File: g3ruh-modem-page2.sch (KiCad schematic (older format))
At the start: 48 parts, among them J8 CONN_01X02, P1 CONN_01X03, P2 CONN_01X06, P3 CONN_01X05, P4 C96ABC, U11 74HC14, U13 74HC86, U14 74HC164, U15 27C128, U16 TL084, U17 74HC74, U18 74HC164, U19 ZN429E-8

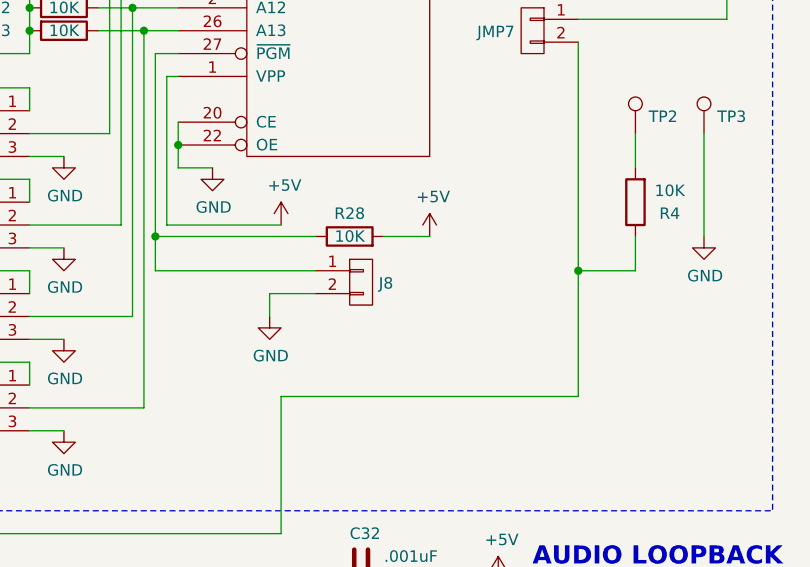
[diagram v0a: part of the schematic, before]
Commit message: Parts in roughly the right places and footprints verified.
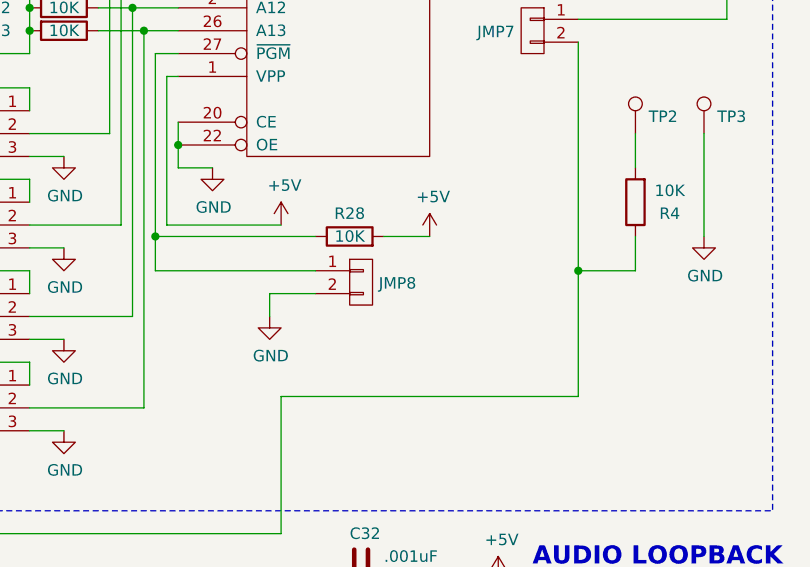
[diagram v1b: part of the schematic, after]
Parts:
- C29, C30, C31, C32: footprint Capacitors_THT:C_Disc_D3.0mm_W2.0mm_P2.50mm -> Capacitors_THT:C_Axial_L3.8mm_D2.6mm_P10.00mm_Horizontal
- renumbered J8 to JMP8
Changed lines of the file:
@@
 $EndComp
 $Comp
-L CONN_01X02 J8
+L CONN_01X02 JMP8
 U 1 1 596FAC32
 P 9350 3200
-F 0 "J8" H 9427 3195 50  0000 L CNN
+F 0 "JMP8" H 9427 3195 50  0000 L CNN
 F 1 "CONN_01X02" H 9428 3150 50  0001 L CNN
 F 2 "Pin_Headers:Pin_Header_Straight_1x02_Pitch2.54mm" H 9350 3200 50  0001 C CNN
@@
 F 0 "C32" V 9200 4400 50  0000 L CNN
 F 1 ".001uF" V 9300 4550 50  0000 L CNN
-F 2 "Capacitors_THT:C_Disc_D3.0mm_W2.0mm_P2.50mm" H 9388 4300 50  0001 C CNN
+F 2 "Capacitors_THT:C_Axial_L3.8mm_D2.6mm_P10.00mm_Horizontal" H 9388 4300 50  0001 C CNN
 F 3 "" H 9350 4450 50  0001 C CNN
 F 4 "2.5% polystyrene" H 9350 4450 60  0001 C CNN "Type"
@@
 F 0 "C30" H 7050 5200 50  0000 L CNN
 F 1 "100pF" H 7000 5100 50  0000 L CNN
-F 2 "Capacitors_THT:C_Disc_D3.0mm_W2.0mm_P2.50mm" H 6938 5000 50  0001 C CNN
+F 2 "Capacitors_THT:C_Axial_L3.8mm_D2.6mm_P10.00mm_Horizontal" H 6938 5000 50  0001 C CNN
 F 3 "" H 6900 5150 50  0001 C CNN
 F 4 "2.5% polystyrene" H 6900 5150 60  0001 C CNN "Type"
@@
 F 0 "C29" H 5200 5200 50  0000 L CNN
 F 1 ".0033" H 5150 5100 50  0000 L CNN
-F 2 "Capacitors_THT:C_Disc_D3.0mm_W2.0mm_P2.50mm" H 5088 5000 50  0001 C CNN
+F 2 "Capacitors_THT:C_Axial_L3.8mm_D2.6mm_P10.00mm_Horizontal" H 5088 5000 50  0001 C CNN
 F 3 "" H 5050 5150 50  0001 C CNN
 F 4 "2.5% polystyrene" H 5050 5150 60  0001 C CNN "Type"
@@
 F 0 "C31" V 6500 4500 50  0000 L CNN
 F 1 "470pF" V 6600 4650 50  0000 L CNN
-F 2 "Capacitors_THT:C_Disc_D3.0mm_W2.0mm_P2.50mm" H 6688 4400 50  0001 C CNN
+F 2 "Capacitors_THT:C_Axial_L3.8mm_D2.6mm_P10.00mm_Horizontal" H 6688 4400 50  0001 C CNN
 F 3 "" H 6650 4550 50  0001 C CNN
 F 4 "2.5% polystyrene" H 6650 4550 60  0001 C CNN "Type"
